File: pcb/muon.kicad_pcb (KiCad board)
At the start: 2 copper layers, 54 x 39 mm, 16 parts, among them J1 Debug Pins, J2 USB_C_Receptacle_USB2.0, SW1 SW_SPST, SW2 SW_SPST, U1 ATSAMD11C14A-SS, U2 MIC5528-3.3YMT-TR

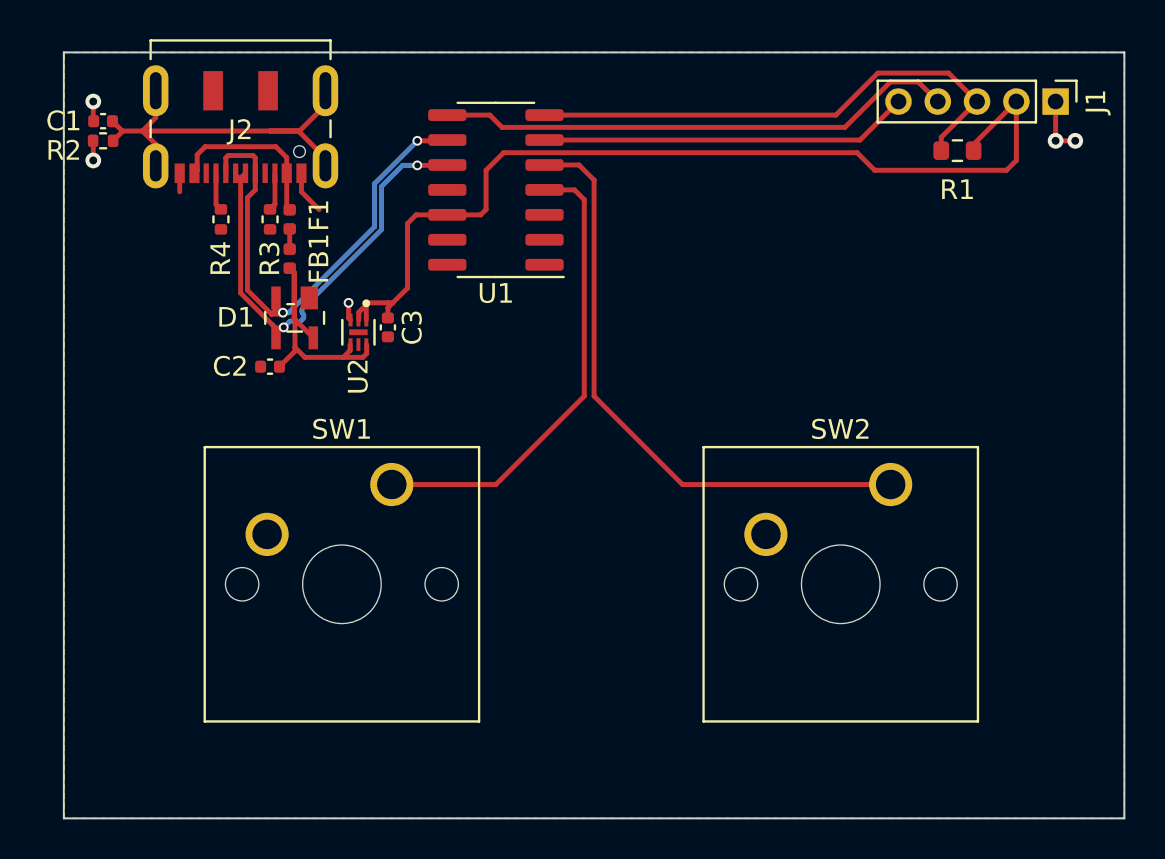
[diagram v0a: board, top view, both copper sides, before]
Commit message: re-route traces for pretty
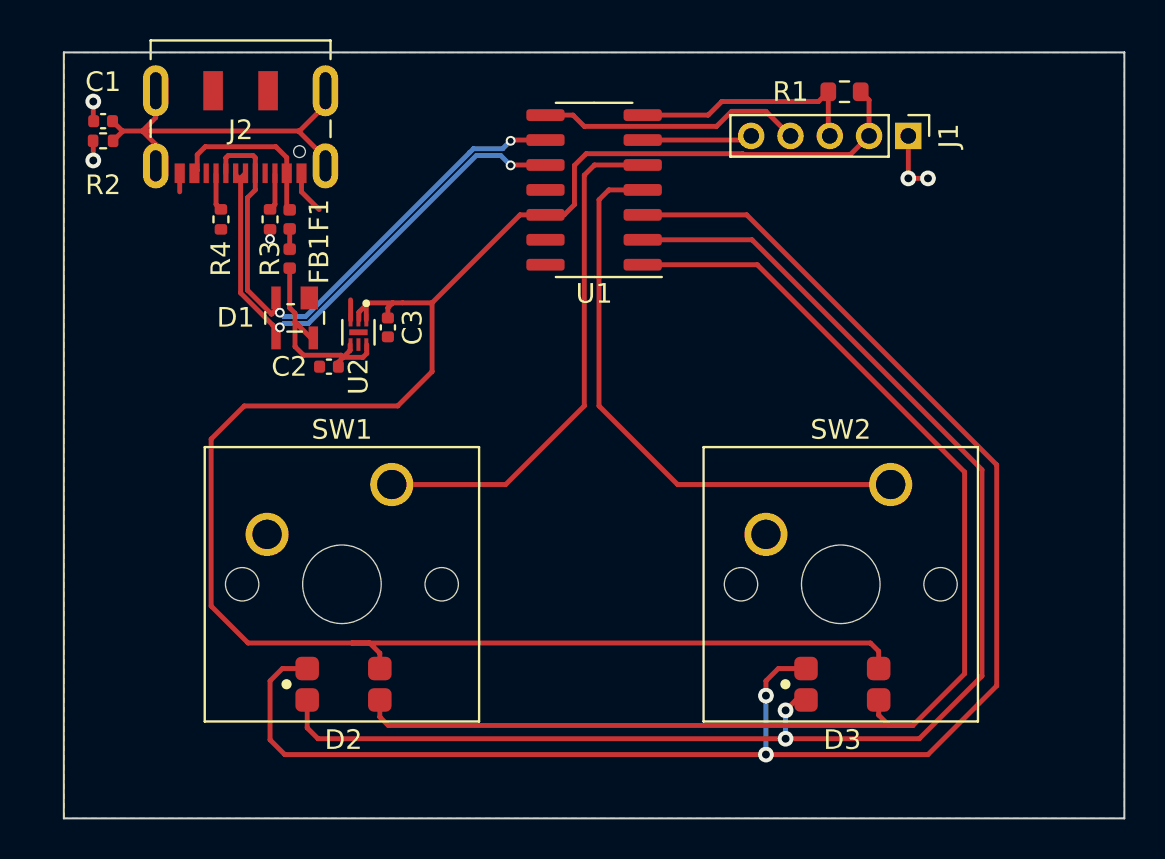
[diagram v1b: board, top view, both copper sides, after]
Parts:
- added D2: LED_RGBA, footprints:156120M173000, F.Cu at (142.2, 90.2)
- added D3: LED_RGBA, footprints:156120M173000, F.Cu at (167.6, 90.2)
- moved J1 7.70 mm to (171.0, 62.2)
- moved R1 6.49 mm to (167.8, 60.0)
- moved U1 5.00 mm to (155.0, 65.0)
- moved C2 3.00 mm to (141.5, 74.0)
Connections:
- U1 pad 1: unconnected-(U1-Pad1) -> /LED_B
- U1 pad 2: unconnected-(U1-Pad2) -> /LED_G
- U1 pad 3: unconnected-(U1-Pad3) -> /LED_R
- U1 pad 4: /SW1 -> /SW2
- U1 pad 5: /SW2 -> /SW1
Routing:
- net /LED_R: track 0.00 -> 84.5 mm, vias 0 -> 2
- net /LED_G: track 0.00 -> 72.7 mm, vias 0 -> 2
- net /LED_B: track 0.00 -> 65.7 mm
- net +3V3: track 49.0 -> 98.3 mm
- net /SWCLK: track 26.8 -> 12.2 mm
- net /RESET: track 18.8 -> 5.61 mm
- net /SWDIO: track 26.6 -> 13.5 mm
- net /D-: track 25.8 -> 30.1 mm
- net /D+: track 23.7 -> 27.7 mm
- net +5V: track 14.7 -> 11.2 mm
- net /SW1: track 23.9 -> 26.4 mm
- net /SH: track 21.2 -> 19.8 mm
- net /SW2: track 30.8 -> 29.4 mm
- net GND: track 9.10 -> 9.86 mm

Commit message: re-route again
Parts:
- SW1, SW2: footprint Button_Switch_Keyboard:SW_Cherry_MX_1.25u_PCB -> Keyswitch:SW_Hotswap_Kailh_MX_1.25u; moved to B.Cu
- moved SW2 6.57 mm to (166.5, 85.5), turned to 180 degrees
- moved SW1 5.84 mm to (142.8, 85.5), turned to 180 degrees
- moved D3 1.14 mm to (166.5, 90.2)
- moved D2 0.51 mm to (142.8, 90.2)
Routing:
- net /SW1: track 26.4 -> 43.5 mm
- net /SW2: track 29.4 -> 32.4 mm
- net /LED_R: track 84.5 -> 86.5 mm
- net /LED_B: track 65.7 -> 66.7 mm
- net /LED_G: track 72.7 -> 73.7 mm
- net GND: vias 5 -> 9

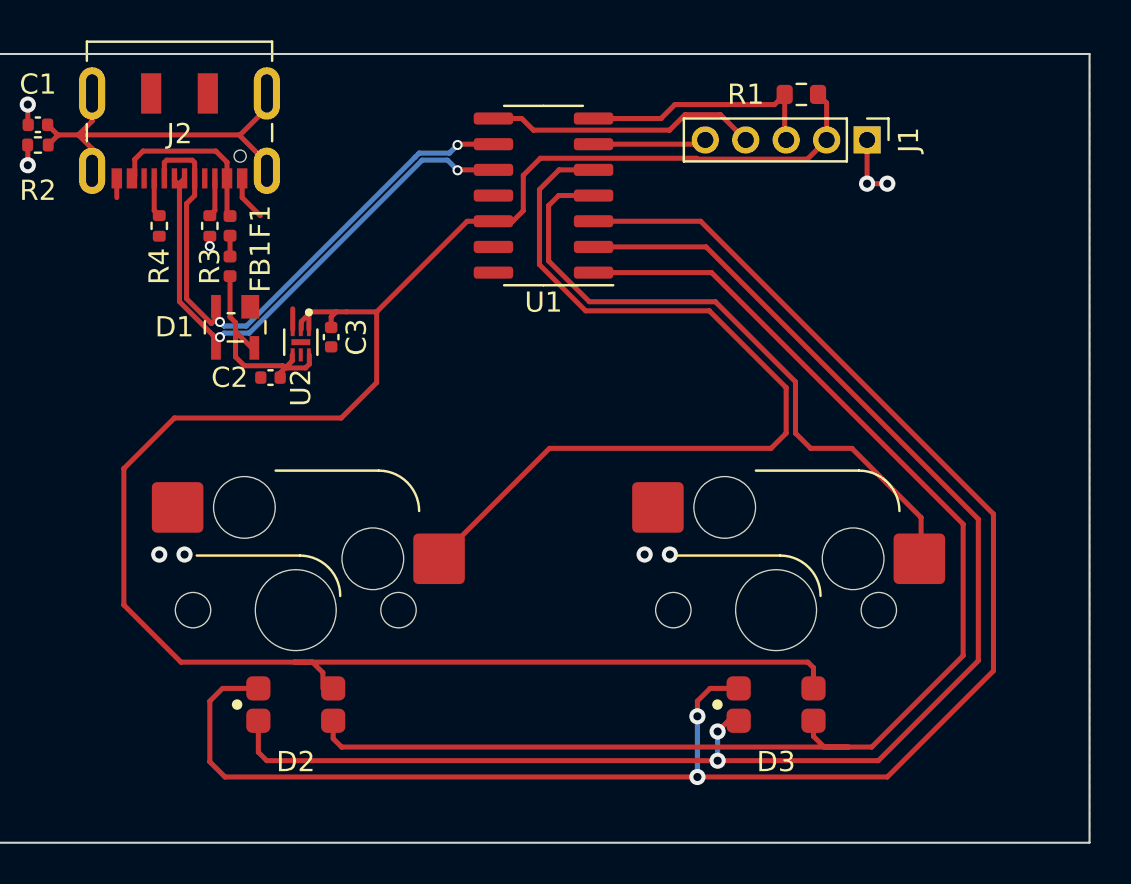
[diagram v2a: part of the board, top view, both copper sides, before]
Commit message: update schematic with proper parts
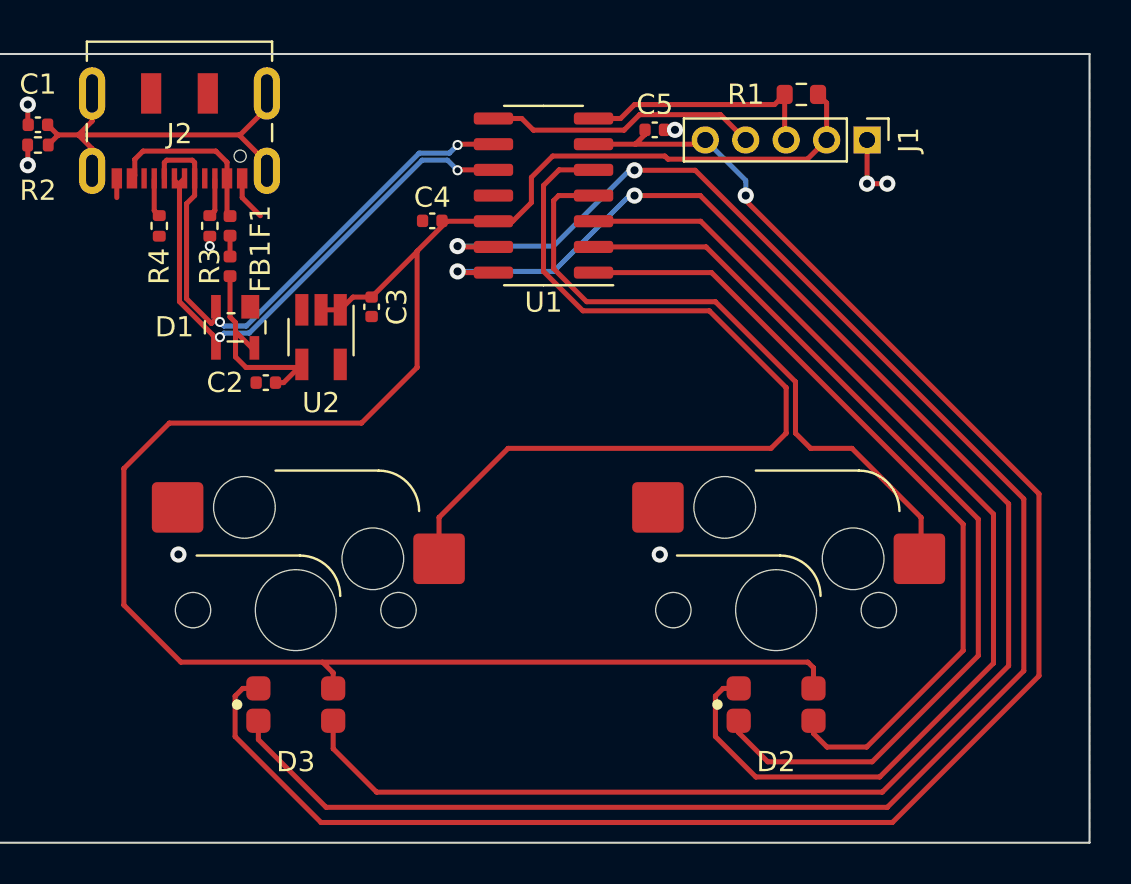
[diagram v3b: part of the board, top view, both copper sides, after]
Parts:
- added C4: 100nF, Capacitor_SMD:C_0402_1005Metric, F.Cu at (149.5, 66.2)
- added C5: 100nF, Capacitor_SMD:C_0402_1005Metric, F.Cu at (160.5, 61.8)
- C2: value 2.2uF -> 1uF
- C3: value 2.2uF -> 4.7uF
- F1: value 500mA -> 150mA
- U2: value MIC5528-3.3YMT-TR -> MIC5317-3.3YM5-TR; footprint MIC55:SON40P120X120X60-7N -> Package_TO_SOT_SMD:SOT-23-5_HandSoldering
- moved C3 2.50 mm to (146.5, 70.5)
- moved U2 1.03 mm to (144.0, 72.0)
- moved C2 0.34 mm to (141.3, 74.2)
- renumbered D3 to D2, D2 to D3
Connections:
- D2 pad 1: /LED_R -> /LED1_R
- D2 pad 2: /LED_G -> /LED1_G
- D2 pad 3: /LED_B -> /LED1_B
- D3 pad 1: /LED_R -> /RESET/LED2_R
- D3 pad 2: /LED_G -> /LED2_G
- D3 pad 3: /LED_B -> /LED2_B
- J1 pad 5: /RESET -> /RESET/LED2_R
- U1 pad 1: /LED_B -> /LED1_B
- U1 pad 13: unconnected-(U1-Pad13) -> /LED2_G
- U1 pad 14: unconnected-(U1-Pad14) -> /LED2_B
- U1 pad 2: /LED_G -> /LED1_G
- U1 pad 3: /LED_R -> /LED1_R
- U1 pad 6: /RESET -> /RESET/LED2_R
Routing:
- net /LED2_G: track 0.00 -> 89.5 mm, vias 0 -> 2
- net /RESET/LED2_R: track 0.00 -> 87.7 mm, vias 0 -> 1
- net /LED_R: track 86.5 -> 0.00 mm, vias 2 -> 0
- net /LED2_B: track 0.00 -> 83.2 mm, vias 0 -> 2
- net /LED_G: track 73.7 -> 0.00 mm, vias 2 -> 0
- net /LED_B: track 66.7 -> 0.00 mm
- net /LED1_R: track 0.00 -> 53.4 mm
- net /LED1_G: track 0.00 -> 46.6 mm
- net /LED1_B: track 0.00 -> 40.0 mm
- net /RESET: track 5.61 -> 0.00 mm
- net /SW1: track 43.5 -> 44.6 mm
- net GND: track 9.86 -> 8.84 mm, vias 9 -> 8
- net +5V: track 11.2 -> 10.6 mm
- net /D-: track 30.1 -> 29.5 mm

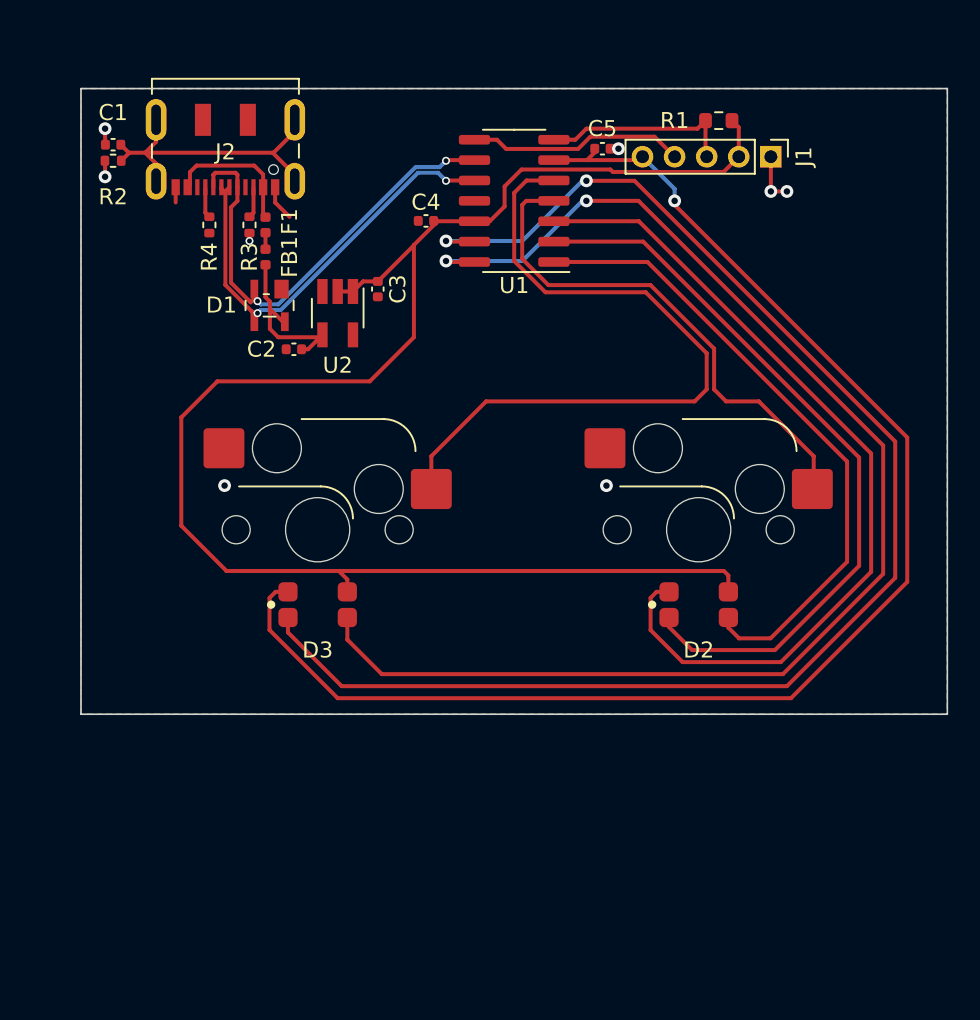
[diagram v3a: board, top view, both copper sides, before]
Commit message: re-route and remove 'uneeded' things
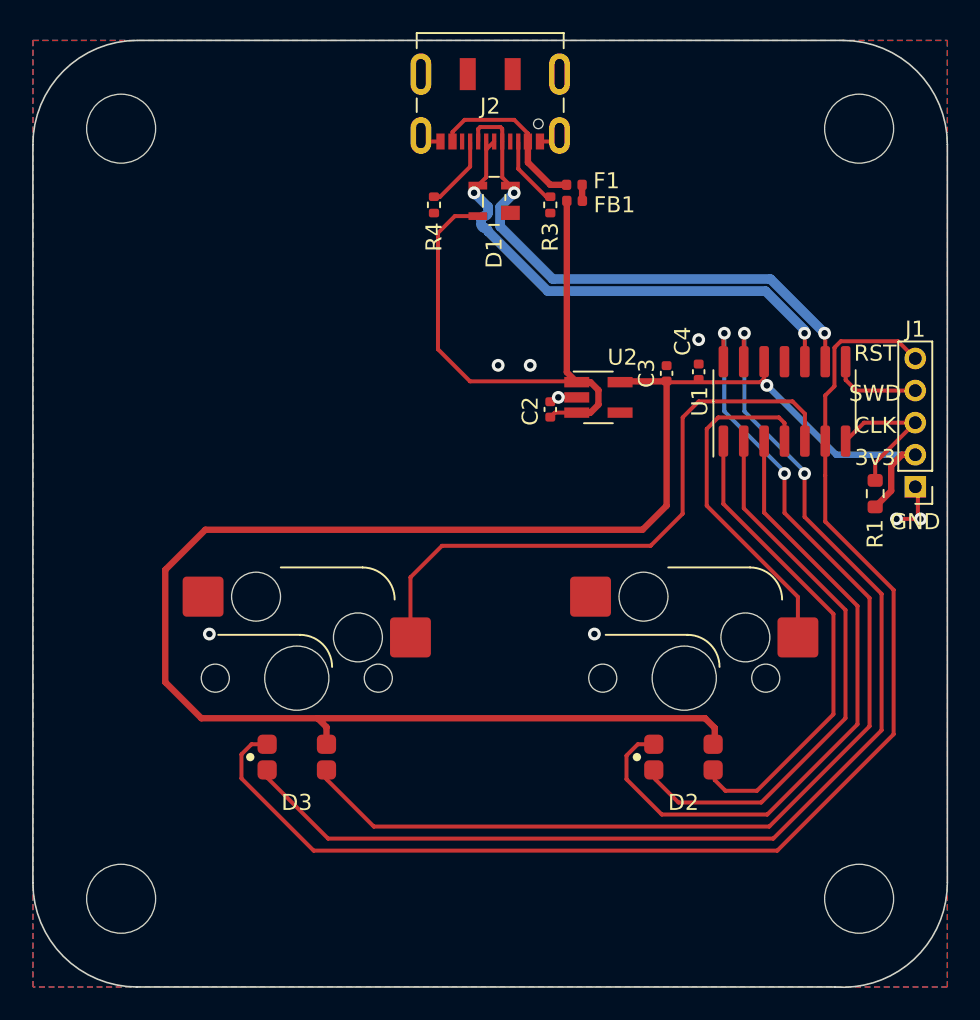
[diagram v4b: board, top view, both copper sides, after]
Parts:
- removed C1, C5: 100nF, Capacitor_SMD:C_0402_1005Metric
- removed R2: 100k, Resistor_SMD:R_0402_1005Metric
- added REF**: MountingHole_4.3mm_M4, MountingHole:MountingHole_4.3mm_M4, F.Cu at (176.5, 60.5)
- added REF**: MountingHole_4.3mm_M4, MountingHole:MountingHole_4.3mm_M4, F.Cu at (130.5, 108.5)
- added REF**: MountingHole_4.3mm_M4, MountingHole:MountingHole_4.3mm_M4, F.Cu at (176.5, 108.5)
- added REF**: MountingHole_4.3mm_M4, MountingHole:MountingHole_4.3mm_M4, F.Cu at (130.5, 60.5)
- moved R1 25.2 mm to (177.5, 83.2), turned to 90 degrees
- moved J1 22.5 mm to (180.0, 82.8), turned to 180 degrees
- moved U1 21.0 mm to (171.8, 77.5), turned to 90 degrees
- moved FB1 19.6 mm to (158.8, 65.0), turned to 180 degrees
- moved C4 19.4 mm to (166.5, 75.7), turned to -90 degrees
- moved F1 19.4 mm to (158.8, 64.0), turned to 180 degrees
- moved R3 18.8 mm to (157.2, 65.2)
- moved C3 18.8 mm to (164.5, 75.8), turned to 90 degrees
- moved U2 17.1 mm to (160.2, 77.2), turned to 0 degrees
- moved J2 16.7 mm to (153.5, 58.2)
- moved C2 16.4 mm to (157.2, 78.0), turned to 90 degrees
- moved D1 15.4 mm to (153.8, 65.0), turned to 90 degrees
- moved R4 14.1 mm to (150.0, 65.2)
- moved D3 9.59 mm to (141.4, 99.7)
- moved D2 9.55 mm to (165.6, 99.7)
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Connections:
- J2 pad S1: /SH -> GND
- U2 pad 1: +3V3 -> +5V
- U2 pad 2: +3V3 -> GND
- U2 pad 3: GND -> +5V
- U2 pad 4: +5V -> unconnected-(U2-Pad4)
- U2 pad 5: unconnected-(U2-Pad5) -> +3V3
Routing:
- net +5V: track 10.6 -> 37.0 mm
- net /SH: track 19.8 -> 0.00 mm
- net /LED2_G: track 89.5 -> 73.2 mm
- net /LED2_B: track 83.2 -> 68.3 mm
- net +3V3: track 98.8 -> 112.6 mm, vias 0 -> 1
- net /LED1_R: track 53.4 -> 41.3 mm
- net /LED1_G: track 46.6 -> 35.1 mm
- net /SW2: track 32.2 -> 21.9 mm
- net /LED1_B: track 40.0 -> 30.1 mm
- net /SWDIO: track 13.5 -> 5.75 mm
- net /RESET/LED2_R: track 87.7 -> 80.6 mm, vias 1 -> 0
- net /SW1: track 44.6 -> 38.4 mm
- net /D-: track 29.5 -> 33.4 mm
- net /D+: track 27.7 -> 31.1 mm
- net /SWCLK: track 12.2 -> 9.45 mm
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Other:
- board size 54 x 39 mm -> 57 x 59 mm
- board text added: "3v3"
- board text added: "CLK"
- board text added: "GND"
- board text added: "RST"
- board text added: "SWD"

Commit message: lots of things
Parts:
- removed D3: LED_RGBA, footprints:156120M173000
- added C1: 5p, Capacitor_SMD:C_0402_1005Metric, F.Cu at (132.2, 70.2)
- added C5: 5p, Capacitor_SMD:C_0402_1005Metric, F.Cu at (129.2, 66.5)
- added C6: 0.1u, Capacitor_SMD:C_0402_1005Metric, F.Cu at (149.7, 83.2)
- added C7: 0.1u, Capacitor_SMD:C_0402_1005Metric, F.Cu at (137.8, 97.5)
- added C8: 0.1u, Capacitor_SMD:C_0402_1005Metric, F.Cu at (175.0, 85.8)
- added C9: 0.1u, Capacitor_SMD:C_0402_1005Metric, F.Cu at (174.2, 96.8)
- added LED1: SK6812MINI-E, marbastlib-various:LED_6028R, F.Cu at (141.5, 86.8)
- added LED2: SK6812MINI-E, marbastlib-various:LED_6028R, F.Cu at (165.2, 86.8)
- added R2: 220, Resistor_SMD:R_0402_1005Metric, F.Cu at (135.3, 85.8)
- added R5: 220, Resistor_SMD:R_0402_1005Metric, F.Cu at (128.8, 95.5)
- added U3: RP2040, rp2040:QFN-56-1EP_7x7mm_P0.4mm_EP3.2x3.2mm, F.Cu at (141.2, 64.5)
- added U4: W25Q80DVSSIG, kicad-w25q-library:W25Q_SOIC-8, F.Cu at (158.0, 25.2)
- added Y1: Crystal_GND24_Small, Crystal:Crystal_SMD_3225-4Pin_3.2x2.5mm, F.Cu at (131.8, 67.6)
- C2: value 1uF -> 10uF
- C3: value 4.7uF -> 10uF
- D1: value PRTR5V0U2X -> WS2812B; footprint footprints:BF994S -> LED_SMD:LED_WS2812B_PLCC4_5.0x5.0mm_P3.2mm
- D2: value LED_RGBA -> WS2812B; footprint footprints:156120M173000 -> LED_SMD:LED_WS2812B_PLCC4_5.0x5.0mm_P3.2mm
- SW1, SW2: value SW_SPST -> SW_Push
- U1: value ATSAMD11C14A-SS -> SRV05-4; footprint Package_SO:SOIC-14_3.9x8.7mm_P1.27mm -> marbastlib-various:SOT-23-6-routable
- U2: value MIC5317-3.3YM5-TR -> AP2112; footprint Package_TO_SOT_SMD:SOT-23-5_HandSoldering -> Package_TO_SOT_SMD:SOT-23-5
- moved C4 60.1 mm to (106.8, 69.5)
- moved C3 51.4 mm to (113.5, 69.2)
- moved U2 51.1 mm to (109.8, 69.5)
- moved C2 42.6 mm to (115.5, 69.5)
- moved J1 40.8 mm to (212.0, 57.5)
- moved D1 35.4 mm to (133.5, 94.0), turned to 180 degrees
- moved U1 21.4 mm to (153.8, 66.0), turned to 180 degrees
- moved R1 13.3 mm to (190.5, 80.2)
- moved SW2 13.0 mm to (165.2, 81.8)
- moved SW1 13.0 mm to (141.5, 81.8)
- moved D2 7.88 mm to (170.8, 93.8), turned to 180 degrees
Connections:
- D1 pad 1: GND -> +5V
- D1 pad 2: /D- -> Net-(D1-Pad2)
- D1 pad 3: /D+ -> GND
- D1 pad 4: +5V -> Net-(D1-Pad4)
- D2 pad 1: /LED1_R -> +5V
- D2 pad 2: /LED1_G -> unconnected-(D2-Pad2)
- D2 pad 3: /LED1_B -> GND
- D2 pad 4: +3V3 -> Net-(D1-Pad2)
- J1 pad 2: +3V3 -> /SWCLK
- J1 pad 3: /SWCLK -> /SWD
- J1 pad 4: /SWDIO -> /~{RESET}
- J1 pad 5: /RESET/LED2_R -> +3V3
- U1 pad 1: /LED1_B -> unconnected-(U1-Pad1)
- U1 pad 2: /LED1_G -> GND
- U1 pad 3: /LED1_R -> /D-
- U1 pad 4: /SW2 -> /D+
- U1 pad 5: /SW1 -> +5V
- U1 pad 6: /RESET/LED2_R -> unconnected-(U1-Pad6)
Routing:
- net +3V3: track 112.6 -> 0.00 mm, vias 1 -> 0
- net /RESET/LED2_R: track 80.6 -> 0.00 mm
- net /LED2_G: track 73.2 -> 0.00 mm, vias 2 -> 0
- net /LED2_B: track 68.3 -> 0.00 mm, vias 2 -> 0
- net /LED1_R: track 41.3 -> 0.00 mm
- net /SW1: track 38.4 -> 0.00 mm
- net /LED1_G: track 35.1 -> 0.00 mm
- net /LED1_B: track 30.1 -> 0.00 mm
- net /D+: track 31.1 -> 4.72 mm, vias 2 -> 0
- net /D-: track 33.4 -> 7.22 mm, vias 2 -> 0
- net /SW2: track 21.9 -> 0.00 mm
- net Net-(LED1-Pad2): track 0.00 -> 18.9 mm
- net +5V: track 37.0 -> 27.4 mm
- net /SWCLK: track 9.45 -> 0.00 mm
- net /XIN: track 0.00 -> 7.87 mm
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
